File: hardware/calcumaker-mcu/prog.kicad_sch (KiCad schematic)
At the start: 1 part, among them J4 SWD TC2030-NL

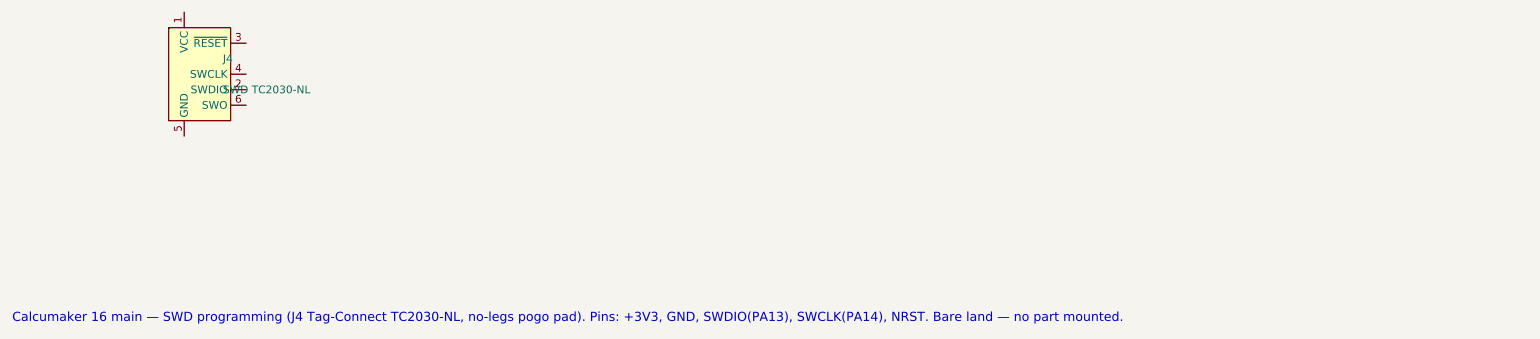
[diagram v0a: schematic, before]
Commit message: hardware: 3-board split (MCU + keyboard + display), wired display, real connectors (#1)
* hardware: 3-board split (MCU + keyboard + display), wired display, real connectors

Split the single logic board into three, wire the display as a KiCad
multi-channel design, and settle every interconnect on real, in-stock parts.

Three-board split (was two):
- Rename calcumaker-main -> calcumaker-mcu (brain/PSU logic board).
- New calcumaker-keyboard board: 50-key Cherry MX matrix + its own
  STM32G031K8U6 scanner (LCSC C432207, UFQFPN-32) + annunciator LEDs,
  mezzanine-stacked above the MCU board. Keyscanning is off the main board;
  only an I2C + UART link + KB_IRQ wake + power cross the mezzanine.

Display board (calcumaker-display):
- Corrected FJ5161AH to a SINGLE-digit 0.56" common-cathode part (C8093) --
  it is NOT a 4-digit module; 48 single digits (16/row x 3), authored symbol
  + 0.56" LTS6760 land. The old 4-digit CC56-12 mapping (and its 3D model)
  was the phantom "clock colon".
- Rebuilt as a KiCad multi-channel design: one reusable display_row.kicad_sch
  (1 TM1640 + 16 digits, fully wired) instantiated x3. Extended kschgen.py
  with wiring primitives + reused-sheet (multi-channel) support.

Connectors (real, verified LCSC / DigiKey parts):
- Display link -> 0.5mm 12P FFC: AFC01-S12FCA-00 (LCSC C262661) on both
  boards; cable = GCT FFC05-TIN 05-12-A-<len>-A-4-06-4-T (DigiKey accessory,
  length TBD). +5V/GND conductors doubled for the display LED current.
- Keyboard mezzanine -> low-profile Hirose DF40 (0.4mm, 2x5, 1.5mm stack):
  DF40C-10DS (C424636) + DF40C-10DP (C424635) -- dedicated KiCad footprint
  + 3D model, unlike the datasheet-less generic parts first considered.

Low-power & wake documented (two Stop domains; keypress -> G0 EXTI wake ->
KB_IRQ -> U575 WKUP; G0 also wakes on I2C address-match). calcumaker-core
is unchanged -- App still consumes (row,col).

All three boards generate + pass the structure check (mcu 52 / keyboard 119 /
display 60 compo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
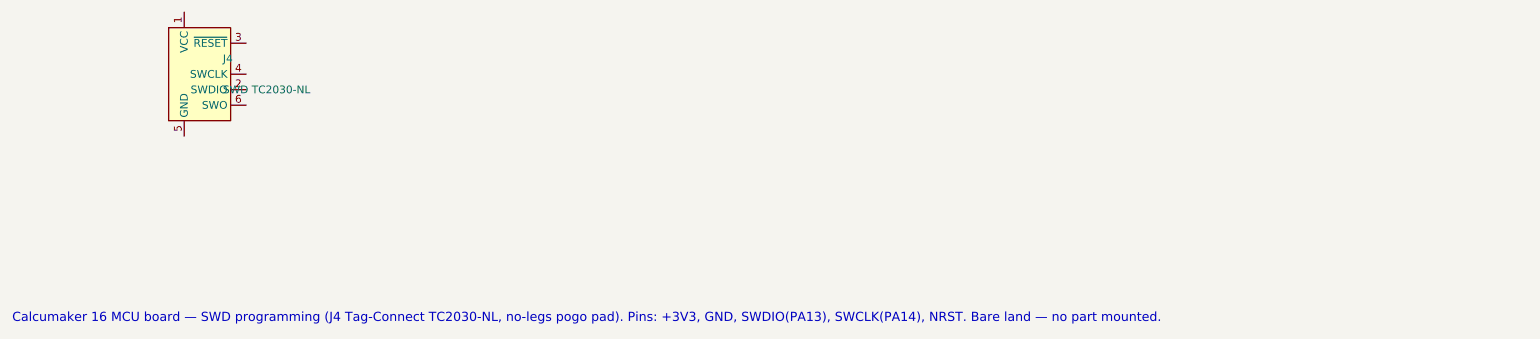
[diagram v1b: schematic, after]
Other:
- note added: "Calcumaker 16 MCU board — SWD programming (J4 Tag-Connect TC2030-NL, no-legs pogo pad). Pins: +3V3, GND, SWDIO(PA13), SWCLK(PA14), NRST. Bare land — no part mounted."
- note removed: "Calcumaker 16 main — SWD programming (J4 Tag-Connect TC2030-NL, no-legs pogo pad). Pins: +3V3, GND, SWDIO(PA13), SWCLK(PA14), NRST. Bare land — no part mounted."
- title: Calcumaker 16 — Main — SWD programming -> Calcumaker 16 — MCU — SWD programming
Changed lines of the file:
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@@
 	(paper "A3")
 	(title_block
-		(title "Calcumaker 16 — Main — SWD programming")
-		(date "2026-06-21")
-		(rev "0.1")
+		(title "Calcumaker 16 — MCU — SWD programming")
+		(date "2026-07-05")
+		(rev "0.2")
 		(company "calcumaker authors")
 	)
@@
 		(pin "6")
 		(instances
-			(project "calcumaker-main"
-				(path "/ca1c0000-0000-4000-8000-00000000ma01/da0f862c-ac78-45d0-9238-36e39d2db74c"
+			(project "calcumaker-mcu"
+				(path "/ca1c0000-0000-4000-8000-00000000ma01/4bb53341-6b5a-4905-9015-f6916355f0f0"
 					(reference "J4")
 					(unit 1)
@@
 		)
 	)
-	(text "Calcumaker 16 main — SWD programming (J4 Tag-Connect TC2030-NL, no-legs pogo pad). Pins: +3V3, GND, SWDIO(PA13), SWCLK(PA14), NRST. Bare land — no part mounted."
+	(text "Calcumaker 16 MCU board — SWD programming (J4 Tag-Connect TC2030-NL, no-legs pogo pad). Pins: +3V3, GND, SWDIO(PA13), SWCLK(PA14), NRST. Bare land — no part mounted."
 		(exclude_from_sim no)
 		(at 15.00 95.00 0)
